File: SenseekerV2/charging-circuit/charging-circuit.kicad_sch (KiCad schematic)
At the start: 73 parts, among them J1 2.54-1*6PHeader-RA, Q1 2N7002, Q2 CJQ4435, Q3 currentmirror, Q4 2N7002, Q5 CJQ4435, Q6 2N7002, Q7 CJQ4435, U1 MAX17048G+T10, U10 BQ25606RGER, U11 Battery Input, U2 MT3608, U3 MT3608, U6 MT3608, U7 2.54-2*20, U8 MAX3232CDBR, U9 ADS1115IDGSR

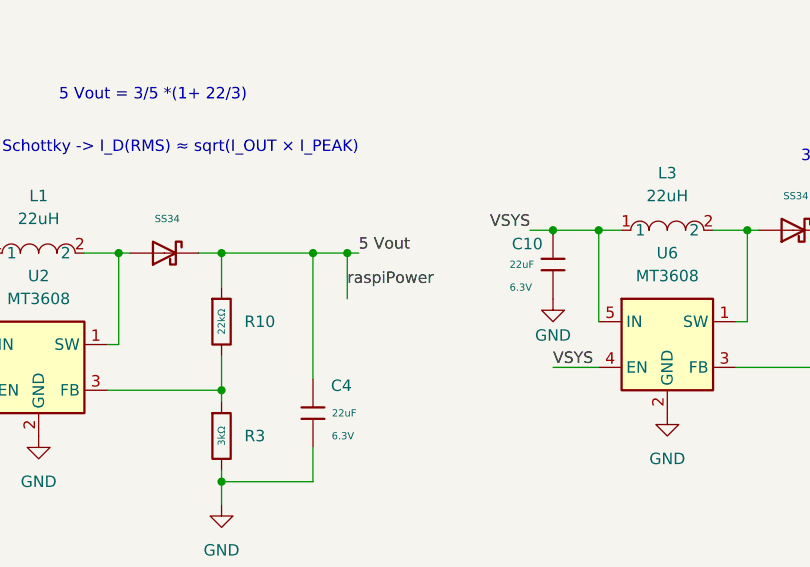
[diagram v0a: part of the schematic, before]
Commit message: Fixed DRC Thermal Errors
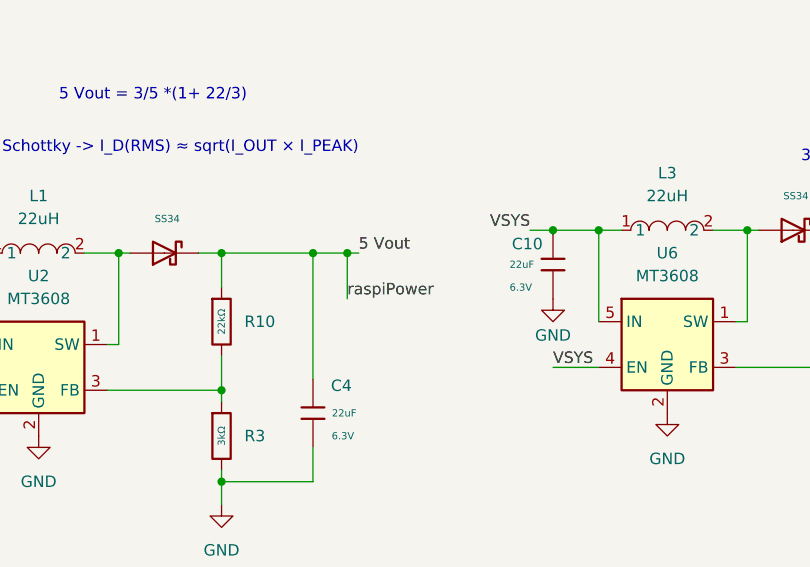
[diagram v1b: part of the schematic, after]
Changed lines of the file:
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@@
+	(wire
+		(pts
+			(xy 185.42 33.02) (xy 185.42 38.1)
+		)
+		(stroke
+			(width 0)
+			(type default)
+		)
+	)
 	(wire
 		(pts
@@
 		(pts
 			(xy 109.22 20.32) (xy 109.22 21.59)
-		)
-		(stroke
-			(width 0)
-			(type default)
-		)
-	)
-	(wire
-		(pts
-			(xy 185.42 33.02) (xy 185.42 38.1)
 		)
 		(stroke
@@
 	)
 	(label "raspiPower"
-		(at 185.42 36.83 0)
-		(effects
-			(font
+		(at 185.42 38.1 0)
+		(effects
+			(font

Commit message: fixed dsub
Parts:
- removed DSub1: DS1037-15FNAKT74-0CC, easyeda2kicad:DSUB-TH_DS1037-15FNAKT74-0CC, symbol easyeda2kicad:DS1037-15FNAKT74-0CC
- added DSub2: DS1038-15FBNSIA74-0CC, easyeda2kicad:DSUB-TH_DS1038-15FBNSIA74-0CC, symbol easyeda2kicad:DS1038-15FBNSIA74-0CC
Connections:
- net GND: now also DSub2.4
- net UART_RX_13V: now also DSub2.1
- net UART_TX_13V: now also DSub2.2
- net at Q7.5 (D), Q7.6 (D), Q7.7 (D)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: now also DSub2.3
- no-connect marks 20 -> 7

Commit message: breakout
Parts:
- removed DSub2: DS1038-15FBNSIA74-0CC, easyeda2kicad:DSUB-TH_DS1038-15FBNSIA74-0CC, symbol easyeda2kicad:DS1038-15FBNSIA74-0CC
- removed Q4, Q6: 2N7002, easyeda2kicad:SOT-23-3_L2.9-W1.3-P1.90-LS2.4-BR, symbol easyeda2kicad:2N7002
- removed Q5, Q7: CJQ4435, easyeda2kicad:SOP-8_L5.0-W4.0-P1.27-LS6.2-BL, symbol easyeda2kicad:CJQ4435
- removed R15, R16: 10kΩ, PCM_JLCPCB:R_0603, symbol PCM_JLCPCB-Resistors:0603,10kΩ
- removed RPROG4, RPROG6: 1kΩ, PCM_JLCPCB:R_0603, symbol PCM_JLCPCB-Resistors:0603,1kΩ
- removed U7: 2.54-2*20, easyeda2kicad:HDR-TH_40P-P2.54-V-F-R2-C20-S2.54, symbol easyeda2kicad:2.54-2*20
- added C3: 100nF, PCM_JLCPCB:C_0603, symbol PCM_JLCPCB-Capacitors:0603,100nF
- added H1, H3, H4: Header-Male-2.54_1x6, easyeda2kicad:HDR-TH_6P-P2.54-V-M-1, symbol easyeda2kicad:Header-Male-2.54_1x6
- added H2: 77311-462K05LF, easyeda2kicad:HDR-TH_5P-P2.54-V-M, symbol easyeda2kicad:77311-462K05LF
- added P1, P2: Header-Male-2.54_2x2, easyeda2kicad:HDR-TH_4P-P2.54-V-M-R2-C2-S2.54-1, symbol easyeda2kicad:Header-Male-2.54_2x2
- added P3, P5, P6, P7: 1.27mm/1*3p, easyeda2kicad:HDR-TH_3P-P1.27-V-M-1, symbol easyeda2kicad:1.27mm_1*3p
- added Q8: CJQ4435, easyeda2kicad:SOP-8_L5.0-W4.0-P1.27-LS6.2-BL, symbol easyeda2kicad:CJQ4435
- added R5: 44.2kohm, easyeda2kicad:R0402, symbol easyeda2kicad:RTT024422FTH
- added R6: 62kohm, easyeda2kicad:R0805, symbol easyeda2kicad:0805W8F6202T5E
- added R7: 30kΩ, PCM_JLCPCB:R_0603, symbol PCM_JLCPCB-Resistors:0603,30kΩ
- added R8, R9: 10kΩ, PCM_JLCPCB:R_0603, symbol PCM_JLCPCB-Resistors:0603,10kΩ
- added RPROG1: 1kΩ, PCM_JLCPCB:R_0603, symbol PCM_JLCPCB-Resistors:0603,1kΩ
- added U4: TPL5110DDCT, easyeda2kicad:TSOT-23-6_L2.9-W1.6-P0.95-LS2.8-BR, symbol easyeda2kicad:TPL5110DDCT
- added U5: BQ25606RGER, easyeda2kicad:VQFN-24_L4.0-W4.0-P0.50-TL-EP2.8, symbol easyeda2kicad:BQ25606RGER
- added U7: Z-21320110021001, easyeda2kicad:HDR-TH_20P-P2.54-V-M-R2-C10-S2.54, symbol easyeda2kicad:Z-21320110021001
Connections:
- net 3.3V: no longer C11.2, D6.1, R18.1
- net D+: now also H2.2; no longer U10.3 (D+)
- net D-: now also H2.1; no longer U10.4 (D-)
- net GND: no longer C1.1, C10.2, C11.1, C12.2, C13.1, C14.1, C15.2, C17.2, C18.2, C2.1, C21.2, C22.1, C4.1, C7.2, C9.1, J1.1, Q1.2 (S), Q3.1 (E), Q3.4 (E), R1.1, R19.2, R22.1, R25.1, R28.2, R29.2, R3.2, R30.2, R31.2, RPROG5.2, U1.1 (CTG), U1.4 (GND), U1.5 (~{ALRT}), U1.6 (QSTRT), U1.9 (EP), U10.17 (GND), U10.18 (GND), U10.25 (EP), U10.6 (OTG), U10.9 (~{CE}), U11.2, U2.2 (GND), U3.2 (GND), U6.2 (GND), U8.15 (GND), U9.1 (ADDR), USBC1.1 (EH), USBC1.2 (EH), USBC1.3 (EH), USBC1.4 (EH), USBC1.A1B12 (GND), USBC1.B1A12 (GND)
- net REGN: no longer R27.1
- net Temp3.3V: now also H4.5
- net UART_RX_13V: now also P1.1
- net UART_TX_13V: now also P1.3
- net VBAT: now also H2.4; no longer C14.2, U1.2 (CELL), U1.3 (VDD), U10.13 (BAT), U10.14 (BAT)
- net VBUS: now also H2.5; no longer C9.2, U10.1 (VAC), U10.24 (VBUS)
- net 12V renamed TEMP12V
- net TEMP12V: now also H4.4; no longer C1.2, D4.1, R2.1
- net 5 Vout renamed 5VOUT
- net 5VOUT: now also P6.2
- net GPIO14/TXD0 renamed TX
- net TX: now also H1.4
- net GPIO15/RXD0 renamed RX
- net RX: now also H1.5
- net GPIO18/PCM.CLK renamed PWMSIG
- net PWMSIG: now also H4.3
- net GPIO2/SDA1 renamed TEMPSDA
- net TEMPSDA: now also H4.2; no longer U1.8 (SDA)
- net GPIO3/SCL1 renamed TEMPSCL
- net TEMPSCL: now also H4.1; no longer U1.7 (SCL)
- removed net VSYS: C10.1, C2.2, C22.2, C7.1, D8.2, D9.2, L1.1, L2.1, L3.1, L4.2, U10.15 (SYS), U10.16 (SYS), U2.4 (EN), U2.5 (IN), U3.4 (EN), U3.5 (IN), U6.4 (EN), U6.5 (IN)
- new net: Q8.4 (G), R9.1, U4.5 (DRV)
- new net: R7.1, U4.3 (DELAY/M_DRV)
- new net: Q8.5 (D), Q8.6 (D), Q8.7 (D), Q8.8 (D), RPROG1.1
- new net 12GND: C1.1, C2.1, P5.3, R1.1, U3.2 (GND)
- new net 12VOUT: C1.2, D4.1, P5.2, R2.1
- new net 12VSYS: C2.2, L2.1, P5.1, U3.4 (EN), U3.5 (IN)
- new net 1D+: H3.2, U10.3 (D+)
- new net 1D-: H3.1, U10.4 (D-)
- new net 2D+: U5.3 (D+), U7.3
- new net 2D-: U5.4 (D-), U7.4
- new net 3V3GND: C10.2, C11.1, P7.3, R19.2, U6.2 (GND)
- new net 3V3VOUT: C11.2, D6.1, P7.2, R18.1
- new net 3V3VSYS: C10.1, L3.1, P7.1, U6.4 (EN), U6.5 (IN)
- new net 5GND: C4.1, C7.2, P6.3, R3.2, U2.2 (GND)
- new net 5VSYS: C7.1, L1.1, P6.1, U2.4 (EN), U2.5 (IN)
- new net Address: C12.2, H4.6, J1.1, Q1.2 (S), Q3.1 (E), Q3.4 (E), RPROG5.2, U9.1 (ADDR)
- new net BAT2: U5.13 (BAT), U5.14 (BAT), U7.13
- new net BTST: U5.21 (BTST), U7.17
- new net CE2: U5.9 (~{CE}), U7.9
- new net DSUB12V: H1.3, P1.4
- new net DSUB3.3V: H1.1
- new net DSUBGND: C17.2, C18.2, C21.2, H1.2, P1.2, U8.15 (GND)
- new net FUELBAT: P2.2, U1.2 (CELL), U1.3 (VDD)
- new net FUELGND: P2.4, U1.1 (CTG), U1.4 (GND), U1.5 (~{ALRT}), U1.6 (QSTRT), U1.9 (EP)
- new net FUELSCL: P2.3, U1.7 (SCL)
- new net FUELSDA: P2.1, U1.8 (SDA)
- new net GND1: C13.1, C14.1, C15.2, C22.1, C9.1, H3.3, R22.1, R25.1, R28.2, R29.2, U10.17 (GND), U10.18 (GND), U10.25 (EP), U10.9 (~{CE})
- new net GND2: U5.17 (GND), U5.18 (GND), U5.25 (EP), U7.15
- new net ICHG2: U5.10 (ICHG), U7.10
- new net ILIM2: U5.8 (ILIM), U7.8
- new net NC2: U5.2 (NC), U7.2
- new net OTG2: U5.6 (OTG), U7.6
- new net PG2: U5.7 (~{PG}), U7.7
- new net PMID2: U5.23 (PMID), U7.19
- new net PWSIG: H1.6
- new net REGN1: R27.1
- new net REGN2: U5.22 (REGN), U7.18
- new net SLEEPGND: C3.2, P3.2, R7.2, R8.2, RPROG1.2, U4.2 (GND)
- new net SLEEPSIG: P3.3
- new net SLEEPSIGNAL: C3.1, R8.1, U4.4 (DONE)
- new net SLEEPVSYS: P3.1, Q8.1 (S), Q8.2 (S), Q8.3 (S), R9.2, U4.1 (VDD), U4.6 (EN/ONE_SHOT)
- new net STAT2: U5.5 (STAT), U7.5
- new net SW2: U5.19 (SW), U5.20 (SW), U7.16
- new net SYS2: U5.15 (SYS), U5.16 (SYS), U7.14
- new net TS2: U5.11 (TS), U7.11
- new net USBGND: H2.3, R30.2, R31.2, U11.2, USBC1.1 (EH), USBC1.2 (EH), USBC1.3 (EH), USBC1.4 (EH), USBC1.A1B12 (GND), USBC1.B1A12 (GND)
- new net VAC2: U5.1 (VAC), U7.1
- new net VBAT1: C14.2, H3.4, U10.13 (BAT), U10.14 (BAT)
- new net VBUS1: C9.2, H3.5, U10.1 (VAC), U10.24 (VBUS)
- new net VBUS2: U5.24 (VBUS), U7.20
- new net VSET2: U5.12 (VSET), U7.12
- new net VSYS1: C22.2, D8.2, D9.2, H3.6, L4.2, U10.15 (SYS), U10.16 (SYS)
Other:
- note added: "Battery can still charge while timer off DONE = rising edge, turn off mosfet and circuit power for sleep timer DONE = low, circuit power on"
- note added: "change to potentionemter"
- note added: "timing resistor for around 2 minutes"
- note removed: "I_REG = 1A - RPROG1 = 1k | SEL = HIGH I_LIMIT = 1.65 A - SEL = HIGH I_TERMINATION = 1000V / RPROG3"
- note removed: "I_TERMINATION = 1000V / 10k = 100mA"
- note removed: "LEDS now turn on with battery or usb c"
- note removed: "Temp3.3V is controlled by GPIO24, will power adc, tempsensor when needed"
- note removed: "VPCC (Voltage Proportional Charge Control) - Input Voltage Regulation) PG (Power Good) - indication to the system that an input source other than the battery is supplying power. TE (Timer Enable) -"
- note removed: "VSET floating for 4.2V charging"
- note removed: "did i switch tx,rx?"
- note removed: "if PG (green) on, good voltage if STAT (red) on, charging"
- note removed: "turn on/off vacuum power with gpio23"
- moved on the sheet: C1, C10, C11, C12, C13, C14, C15, C16, C17, C18, C19, C2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
